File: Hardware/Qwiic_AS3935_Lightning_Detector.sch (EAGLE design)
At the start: 28 parts, among them U1 AS3935

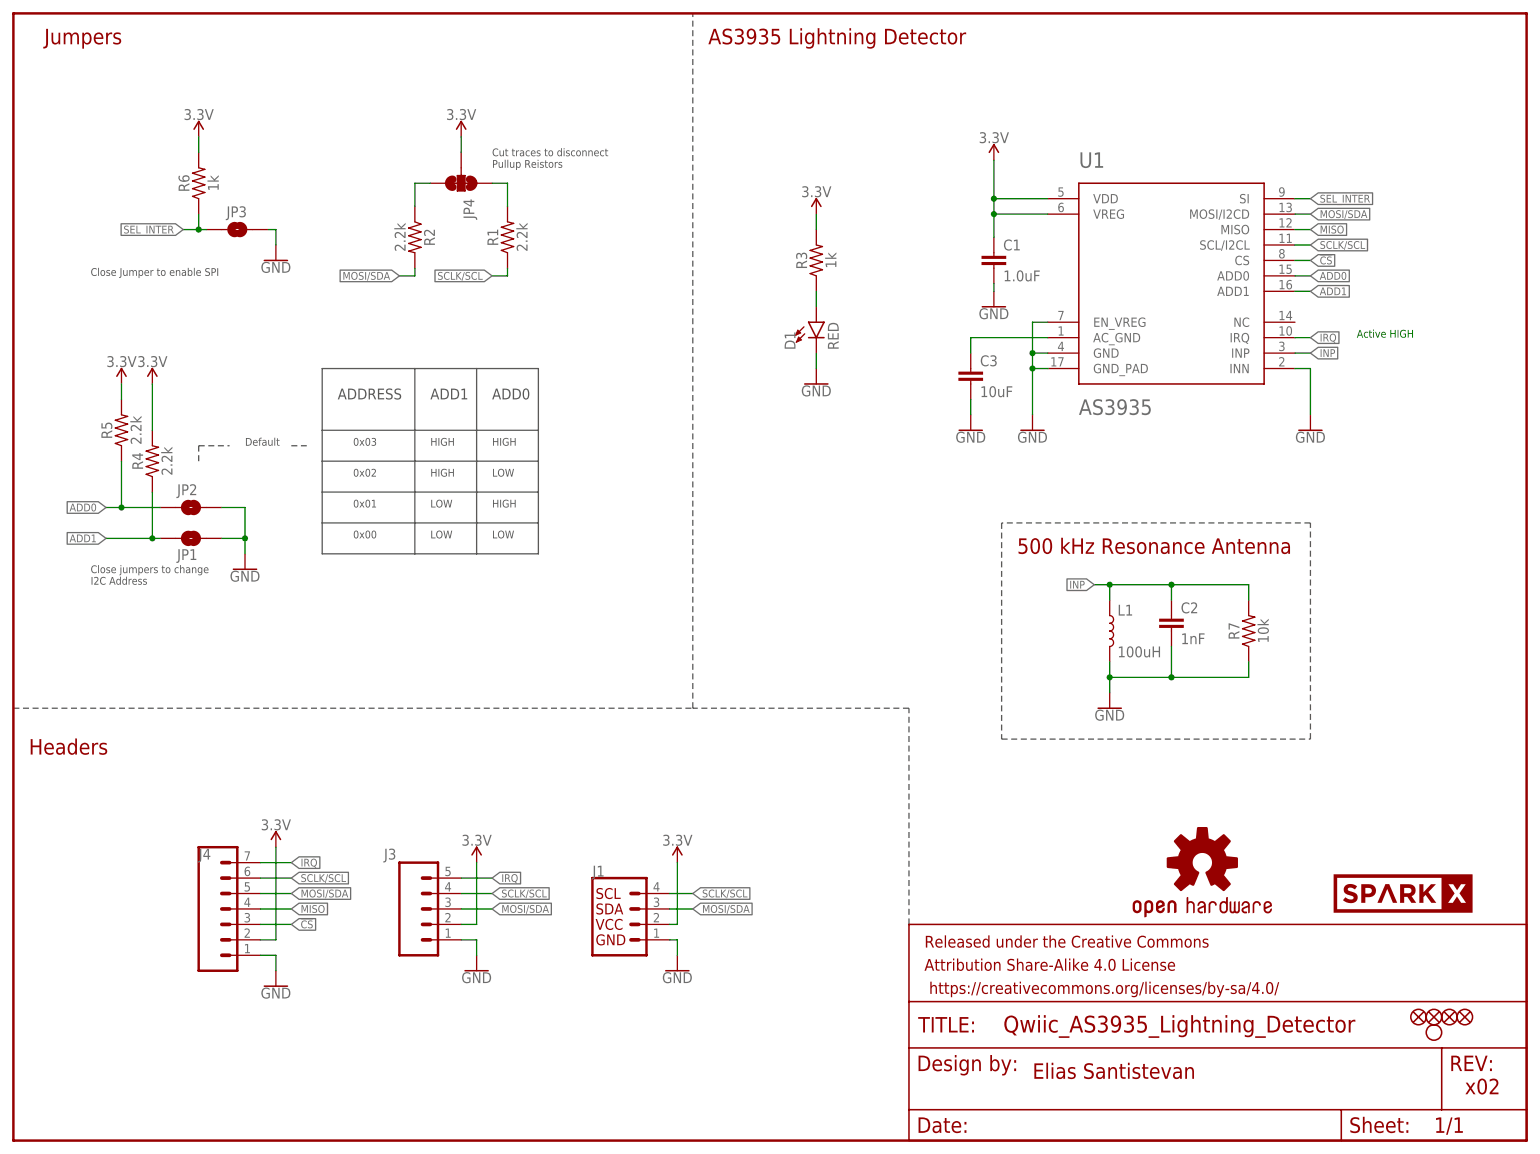
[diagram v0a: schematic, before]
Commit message: Adds SparkFun related silk, adds parts that were added to Eagle libraries
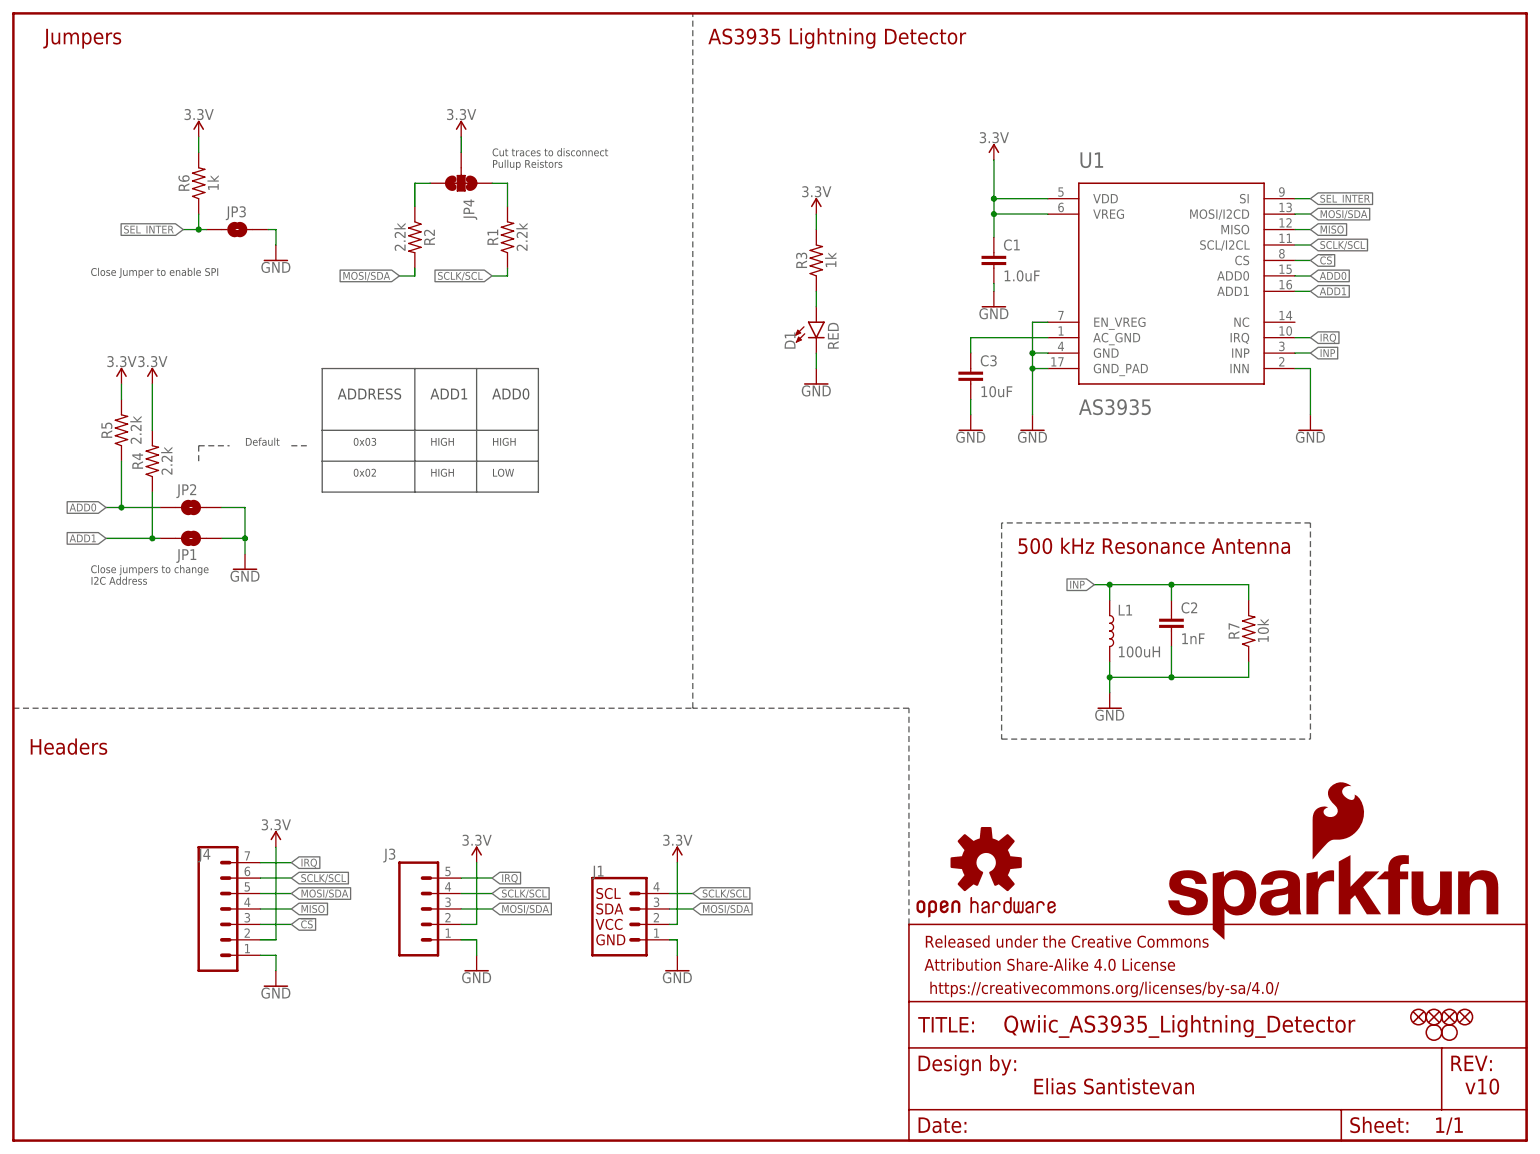
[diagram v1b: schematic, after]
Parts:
- removed U$1: SPARKX-LOGO2, SparkX:SPARKX-LOGO2
- added H2: STAND-OFFTIGHT, SparkFun-Hardware:STAND-OFFTIGHT
- added LOGO2: SFE_LOGO_NAME.1_INCH, SparkFun-Aesthetics:SFE_LOGO_NAME.1_INCH
- added LOGO3: SFE_LOGO_FLAME.1_INCH, SparkFun-Aesthetics:SFE_LOGO_FLAME.1_INCH
- L1: device temp_parts:MA5532-AE -> SparkFun-Coils:MA5532-AE
- U1: device temp_parts:AS3935QFN -> SparkFun-IC-Special-Function:AS3935QFN
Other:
- note added: "v10"
- note removed: "0x00"
- note removed: "0x01"
- note removed: "Active HIGH"
- note removed: "x02"
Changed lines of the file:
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@@
 <part name="SUPPLY12" library="SparkFun-PowerSymbols" deviceset="3.3V" device=""/>
 <part name="LOGO1" library="SparkFun-Aesthetics" deviceset="OSHW-LOGO" device="S"/>
-<part name="U$1" library="SparkX" deviceset="SPARKX-LOGO" device="2"/>
 <part name="C2" library="SparkFun-Capacitors" deviceset="1.0NF/1000PF" device="-0603-50V-10%" value="1nF"/>
 <part name="C3" library="SparkFun-Capacitors" deviceset="10UF" device="-0603-6.3V-20%" value="10uF"/>
@@
 <part name="GND11" library="SparkFun-PowerSymbols" deviceset="GND" device=""/>
 <part name="GND12" library="SparkFun-PowerSymbols" deviceset="GND" device=""/>
-<part name="L1" library="temp_parts" deviceset="MA5532-AE" device="" value="100uH"/>
-<part name="U1" library="temp_parts" deviceset="AS3935" device="QFN" value="AS3935"/>
+<part name="L1" library="SparkFun-Coils" deviceset="MA5532-AE" device="" value="100uH"/>
+<part name="U1" library="SparkFun-IC-Special-Function" deviceset="AS3935" device="QFN" value="AS3935"/>
+<part name="LOGO2" library="SparkFun-Aesthetics" deviceset="SFE_LOGO_NAME" device=".1_INCH"/>
+<part name="LOGO3" library="SparkFun-Aesthetics" deviceset="SFE_LOGO_FLAME" device=".1_INCH"/>
+<part name="H2" library="SparkFun-Hardware" deviceset="STAND-OFF" device="TIGHT"/>
 </parts>
 <sheets>
 <sheet>
 <plain>
-<text x="167.64" y="10.16" size="2.54" layer="94" font="vector">Elias Santistevan</text>
-<text x="238.76" y="7.62" size="2.54" layer="94" font="vector">x02</text>
-<text x="220.98" y="132.08" size="1.27" layer="91" font="vector">Active HIGH</text>
+<text x="167.64" y="7.62" size="2.54" layer="94" font="vector">Elias Santistevan</text>
+<text x="238.76" y="7.62" size="2.54" layer="94" font="vector">v10</text>
 <wire x1="0" y1="71.12" x2="111.76" y2="71.12" width="0.2032" layer="97" style="shortdash"/>
 <wire x1="111.76" y1="71.12" x2="111.76" y2="185.42" width="0.2032" layer="97" style="shortdash"/>
@@
 <wire x1="50.8" y1="116.84" x2="50.8" y2="111.76" width="0.2032" layer="97"/>
 <wire x1="50.8" y1="111.76" x2="50.8" y2="106.68" width="0.2032" layer="97"/>
-<wire x1="50.8" y1="106.68" x2="50.8" y2="101.6" width="0.2032" layer="97"/>
-<wire x1="50.8" y1="101.6" x2="50.8" y2="96.52" width="0.2032" layer="97"/>
-<wire x1="50.8" y1="96.52" x2="66.04" y2="96.52" width="0.2032" layer="97"/>
-<wire x1="66.04" y1="96.52" x2="76.2" y2="96.52" width="0.2032" layer="97"/>
-<wire x1="76.2" y1="96.52" x2="86.36" y2="96.52" width="0.2032" layer="97"/>
-<wire x1="86.36" y1="96.52" x2="86.36" y2="101.6" width="0.2032" layer="97"/>
-<wire x1="86.36" y1="101.6" x2="86.36" y2="106.68" width="0.2032" layer="97"/>
 <wire x1="86.36" y1="106.68" x2="86.36" y2="111.76" width="0.2032" layer="97"/>
 <wire x1="86.36" y1="111.76" x2="86.36" y2="116.84" width="0.2032" layer="97"/>
@@
 <wire x1="76.2" y1="127" x2="66.04" y2="127" width="0.2032" layer="97"/>
 <wire x1="66.04" y1="127" x2="50.8" y2="127" width="0.2032" layer="97"/>
-<wire x1="66.04" y1="127" x2="66.04" y2="96.52" width="0.2032" layer="97"/>
+<wire x1="66.04" y1="127" x2="66.04" y2="106.68" width="0.2032" layer="97"/>
 <wire x1="50.8" y1="116.84" x2="86.36" y2="116.84" width="0.2032" layer="97"/>
 <wire x1="50.8" y1="111.76" x2="86.36" y2="111.76" width="0.2032" layer="97"/>
 <wire x1="50.8" y1="106.68" x2="86.36" y2="106.68" width="0.2032" layer="97"/>
-<wire x1="76.2" y1="127" x2="76.2" y2="96.52" width="0.2032" layer="97"/>
+<wire x1="76.2" y1="127" x2="76.2" y2="106.68" width="0.2032" layer="97"/>
 <text x="78.74" y="121.92" size="1.778" layer="97" font="vector" ratio="15">ADD0</text>
 <text x="68.58" y="121.92" size="1.778" layer="97" font="vector" ratio="15">ADD1</text>
 <text x="68.58" y="114.3" size="1.27" layer="97" font="vector">HIGH</text>
-<text x="68.58" y="99.06" size="1.27" layer="97" font="vector">LOW</text>
 <text x="78.74" y="114.3" size="1.27" layer="97" font="vector">HIGH</text>
-<text x="68.58" y="104.14" size="1.27" layer="97" font="vector">LOW</text>
 <text x="68.58" y="109.22" size="1.27" layer="97" font="vector">HIGH</text>
-<text x="78.74" y="104.14" size="1.27" layer="97" font="vector">HIGH</text>
 <text x="78.74" y="109.22" size="1.27" layer="97" font="vector">LOW</text>
-<text x="78.74" y="99.06" size="1.27" layer="97" font="vector">LOW</text>
-<wire x1="50.8" y1="101.6" x2="86.36" y2="101.6" width="0.2032" layer="97"/>
 <text x="53.34" y="121.92" size="1.778" layer="97" font="vector" ratio="15">ADDRESS</text>
 <text x="55.88" y="114.3" size="1.27" layer="97" font="vector">0x03</text>
 <text x="55.88" y="109.22" size="1.27" layer="97" font="vector">0x02</text>
-<text x="55.88" y="104.14" size="1.27" layer="97" font="vector">0x01</text>
-<text x="55.88" y="99.06" size="1.27" layer="97" font="vector">0x00</text>
 <text x="38.1" y="114.3" size="1.27" layer="97" font="vector" ratio="15">Default</text>
 <wire x1="30.48" y1="111.76" x2="30.48" y2="114.3" width="0.2032" layer="97" style="shortdash"/>
@@
 <attribute name="VALUE" x="43.18" y="51.054" size="1.778" layer="96" align="bottom-center"/>
 </instance>
-<instance part="LOGO1" gate="G$1" x="195.58" y="45.72" smashed="yes"/>
-<instance part="U$1" gate="G$1" x="228.6" y="40.64" smashed="yes"/>
+<instance part="LOGO1" gate="G$1" x="160.02" y="45.72" smashed="yes"/>
 <instance part="C2" gate="G$1" x="190.5" y="83.82" smashed="yes">
 <attribute name="NAME" x="192.024" y="86.741" size="1.778" layer="95" font="vector"/>
@@
 <attribute name="VALUE" x="175.26" y="119.38" size="2.54" layer="96" font="vector" ratio="15"/>
 </instance>
+<instance part="LOGO2" gate="G$1" x="187.96" y="33.02" smashed="yes"/>
+<instance part="LOGO3" gate="G$1" x="213.36" y="45.72" smashed="yes"/>
+<instance part="H2" gate="G$1" x="236.22" y="17.78" smashed="yes"/>
 </instances>
 <busses>

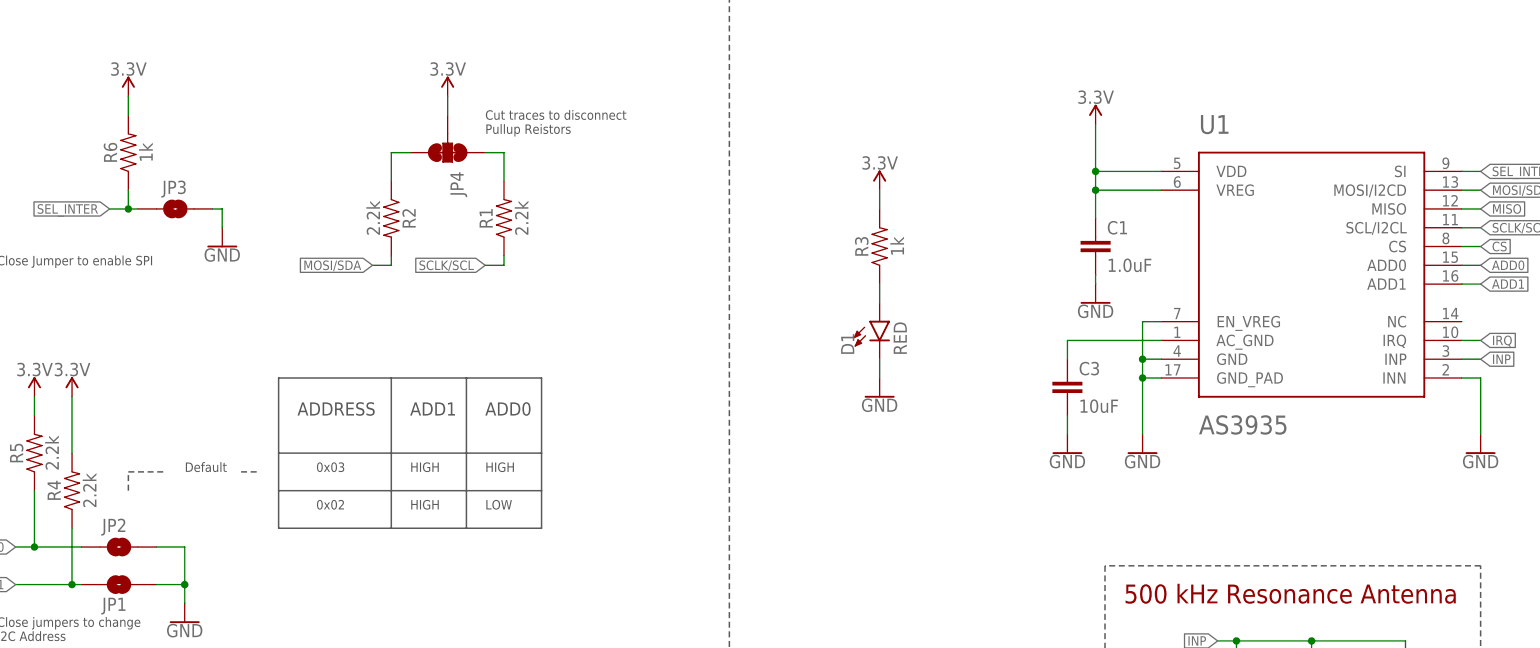
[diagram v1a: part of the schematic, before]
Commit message: Replaces lightning detector - lightning detector was moved to correct library and so needed to be replaced in design
* Changes pull up resistor on the select interface line with a 10k
* Changes the wording of the address info box in the schematic to open/close rather
  than high/low
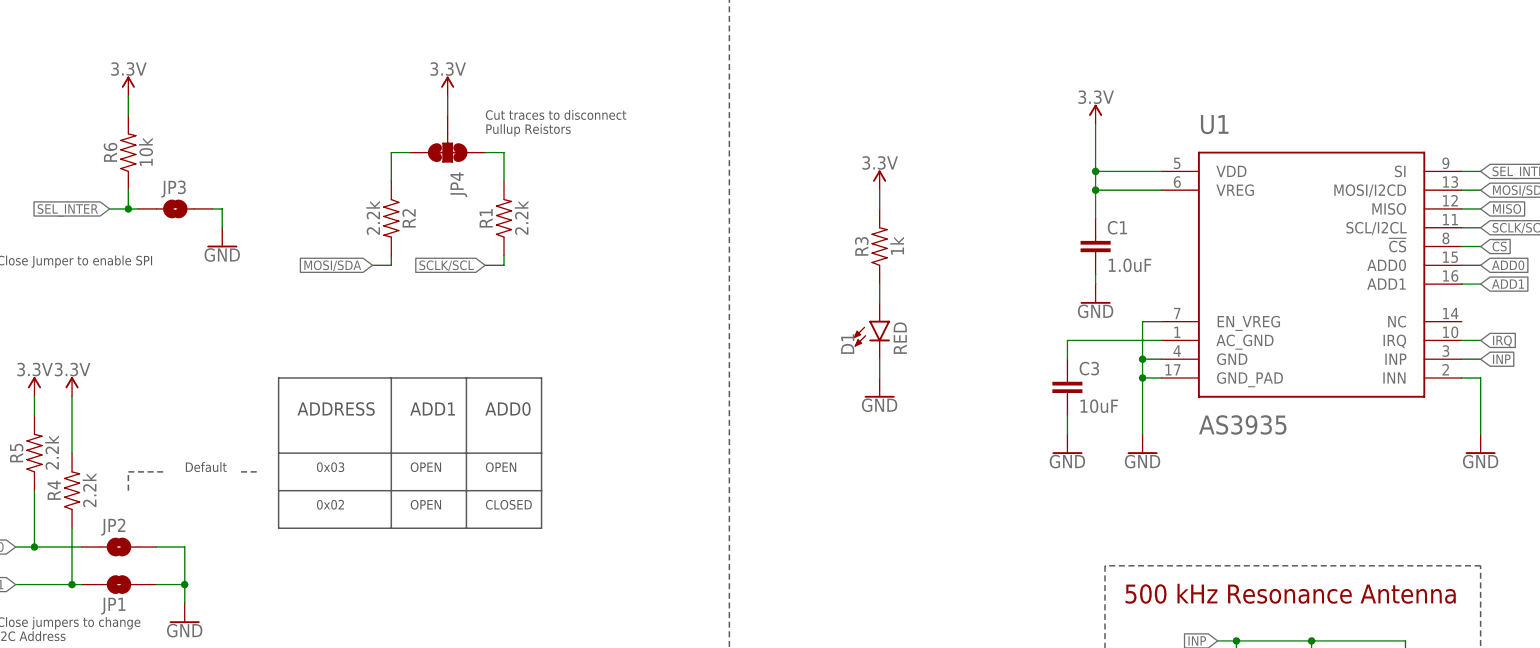
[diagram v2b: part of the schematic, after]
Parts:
- R6: value 1k -> 10k; device SparkFun-Resistors:1KOHM-0603-1/10W-1% -> SparkFun-Resistors:10KOHM-0603-1/10W-1%
- U1: device SparkFun-IC-Special-Function:AS3935QFN -> SparkFun-Sensors:AS3935QFN
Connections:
- net !CS: now also U1.!CS; no longer U1.CS
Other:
- note added: "CLOSED"
- note added: "OPEN"
- note removed: "HIGH"
- note removed: "LOW"
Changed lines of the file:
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@@
 <part name="SUPPLY6" library="SparkFun-PowerSymbols" deviceset="3.3V" device=""/>
 <part name="GND4" library="SparkFun-PowerSymbols" deviceset="GND" device=""/>
-<part name="R6" library="SparkFun-Resistors" deviceset="1KOHM" device="-0603-1/10W-1%" value="1k"/>
+<part name="R6" library="SparkFun-Resistors" deviceset="10KOHM" device="-0603-1/10W-1%" value="10k"/>
 <part name="JP3" library="SparkFun-Jumpers" deviceset="JUMPER-SMT_2_NO" device="_SILK"/>
 <part name="GND5" library="SparkFun-PowerSymbols" deviceset="GND" device=""/>
@@
 <part name="GND12" library="SparkFun-PowerSymbols" deviceset="GND" device=""/>
 <part name="L1" library="SparkFun-Coils" deviceset="MA5532-AE" device="" value="100uH"/>
-<part name="U1" library="SparkFun-IC-Special-Function" deviceset="AS3935" device="QFN" value="AS3935"/>
+<part name="U1" library="SparkFun-Sensors" deviceset="AS3935" device="QFN" value="AS3935"/>
 <part name="LOGO2" library="SparkFun-Aesthetics" deviceset="SFE_LOGO_NAME" device=".1_INCH"/>
 <part name="LOGO3" library="SparkFun-Aesthetics" deviceset="SFE_LOGO_FLAME" device=".1_INCH"/>
@@
 <text x="78.74" y="121.92" size="1.778" layer="97" font="vector" ratio="15">ADD0</text>
 <text x="68.58" y="121.92" size="1.778" layer="97" font="vector" ratio="15">ADD1</text>
-<text x="68.58" y="114.3" size="1.27" layer="97" font="vector">HIGH</text>
-<text x="78.74" y="114.3" size="1.27" layer="97" font="vector">HIGH</text>
-<text x="68.58" y="109.22" size="1.27" layer="97" font="vector">HIGH</text>
-<text x="78.74" y="109.22" size="1.27" layer="97" font="vector">LOW</text>
+<text x="68.58" y="114.3" size="1.27" layer="97" font="vector">OPEN</text>
+<text x="78.74" y="114.3" size="1.27" layer="97" font="vector">OPEN</text>
+<text x="68.58" y="109.22" size="1.27" layer="97" font="vector">OPEN</text>
+<text x="78.74" y="109.22" size="1.27" layer="97" font="vector">CLOSED</text>
 <text x="53.34" y="121.92" size="1.778" layer="97" font="vector" ratio="15">ADDRESS</text>
 <text x="55.88" y="114.3" size="1.27" layer="97" font="vector">0x03</text>
@@
 <wire x1="210.82" y1="144.78" x2="213.36" y2="144.78" width="0.1524" layer="91"/>
 <label x="213.36" y="144.78" size="1.27" layer="95" font="vector" xref="yes"/>
-<pinref part="U1" gate="G$1" pin="CS"/>
-</segment>
-</net>
+<pinref part="U1" gate="G$1" pin="!CS"/>
+</segment>
+</net>
